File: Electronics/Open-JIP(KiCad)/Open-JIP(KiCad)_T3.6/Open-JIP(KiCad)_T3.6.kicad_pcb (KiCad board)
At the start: 2 copper layers, 61.7 x 35.3 mm, 34 parts, among them J1 EJ503A, J2 Screw_Terminal_01x02, U1 74HC4066D,653, U2 74HC4066D,653, U3 KA7812ETU, U4 OPA320AIDBVT, U5 Teensy3.6

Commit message: finished v0.3 for teensy 3.2 and added gerber files
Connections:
- C5 pad 2: Net-(C5-Pad2) -> GNDA
- U4 pad 2: Net-(C5-Pad2) -> GNDA
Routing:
- net GNDA: track 3.68 -> 11.3 mm
- net Net-(C5-Pad2): track 5.68 -> 0.00 mm
- net (no net): vias 2 -> 1

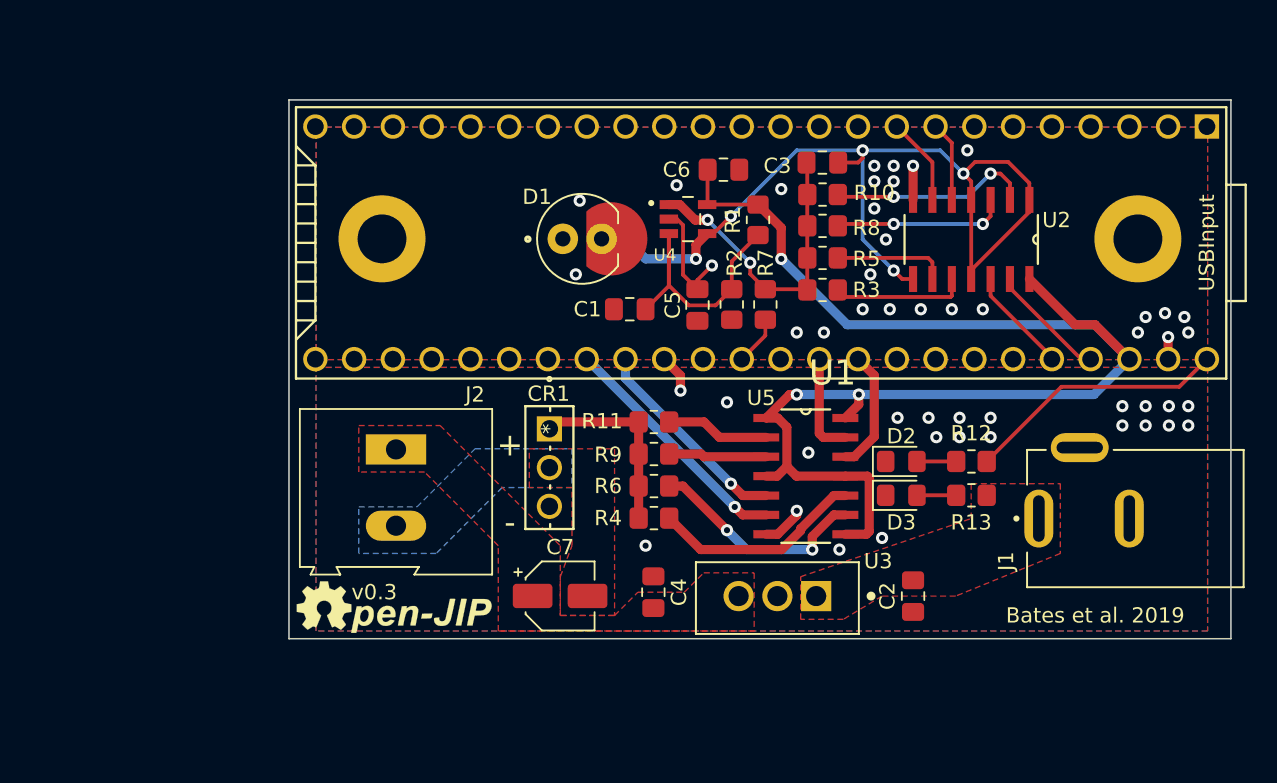
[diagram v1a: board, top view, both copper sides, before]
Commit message: added J-step measuring procedure
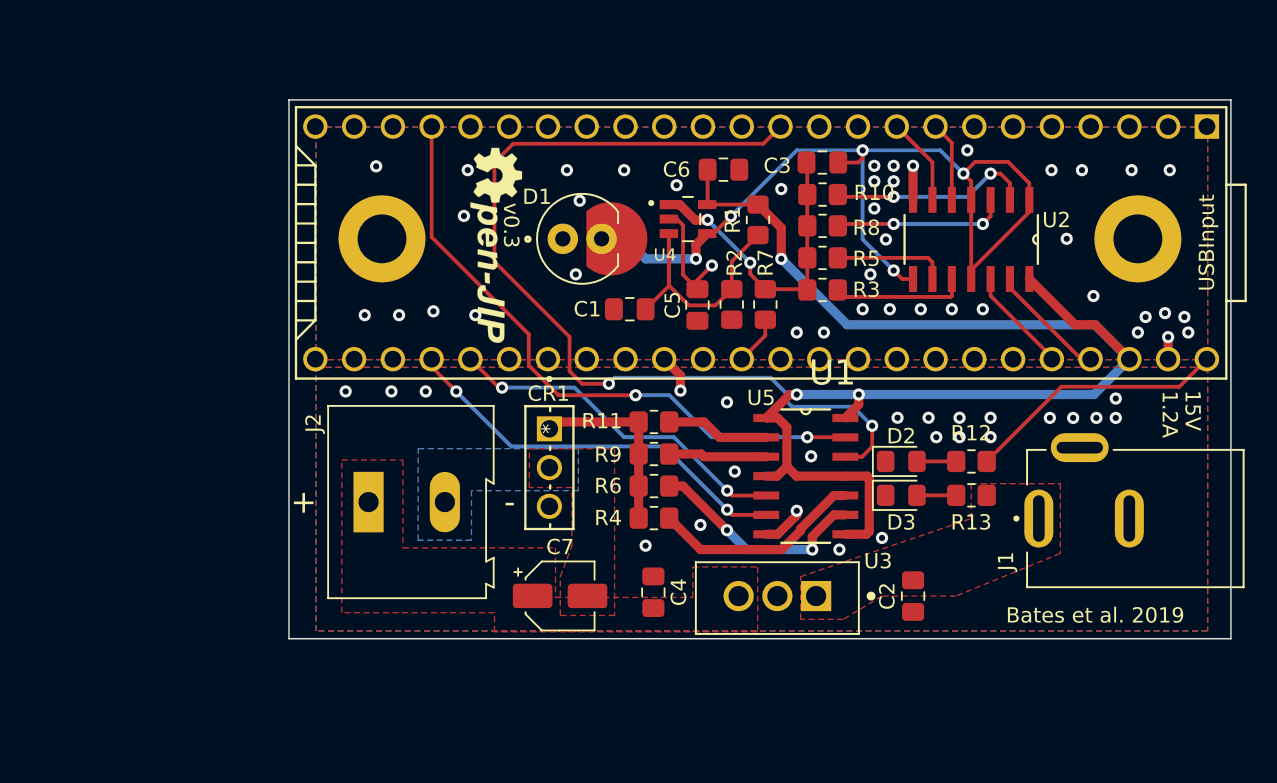
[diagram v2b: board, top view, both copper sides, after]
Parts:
- moved G*** 24.7 mm to (142.8, 82.4), turned to 270 degrees
- moved J2 3.89 mm to (134.5, 99.2), turned to 0 degrees
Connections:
- U5 pad 12: Net-(U5-Pad12) -> ActinicGain4
- U5 pad 21: Net-(U5-Pad21) -> ActinicGain1
- U5 pad 33: Net-(U5-Pad33) -> ActinicGain3
- U5 pad 34: Net-(U5-Pad34) -> ActinicGain2
- U5 pad 37: ActinicGain3 -> Net-(U5-Pad37)
- U5 pad 38: ActinicGain2 -> Net-(U5-Pad38)
- U5 pad 43: ActinicGain1 -> Net-(U5-Pad43)
- U5 pad 44: ActinicGain4 -> Net-(U5-Pad44)
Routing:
- net ActinicGain4: track 7.97 -> 60.8 mm, vias 0 -> 2
- net ActinicGain1: track 6.68 -> 41.0 mm, vias 0 -> 2
- net ActinicGain3: track 16.0 -> 26.4 mm, vias 1 -> 2
- net ActinicGain2: track 13.7 -> 23.1 mm, vias 1 -> 2
- net GNDA: vias 26 -> 41
- net GND: vias 22 -> 24
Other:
- board text added: "1.2A"
- board text added: "15V"

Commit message: od and fluorometer design
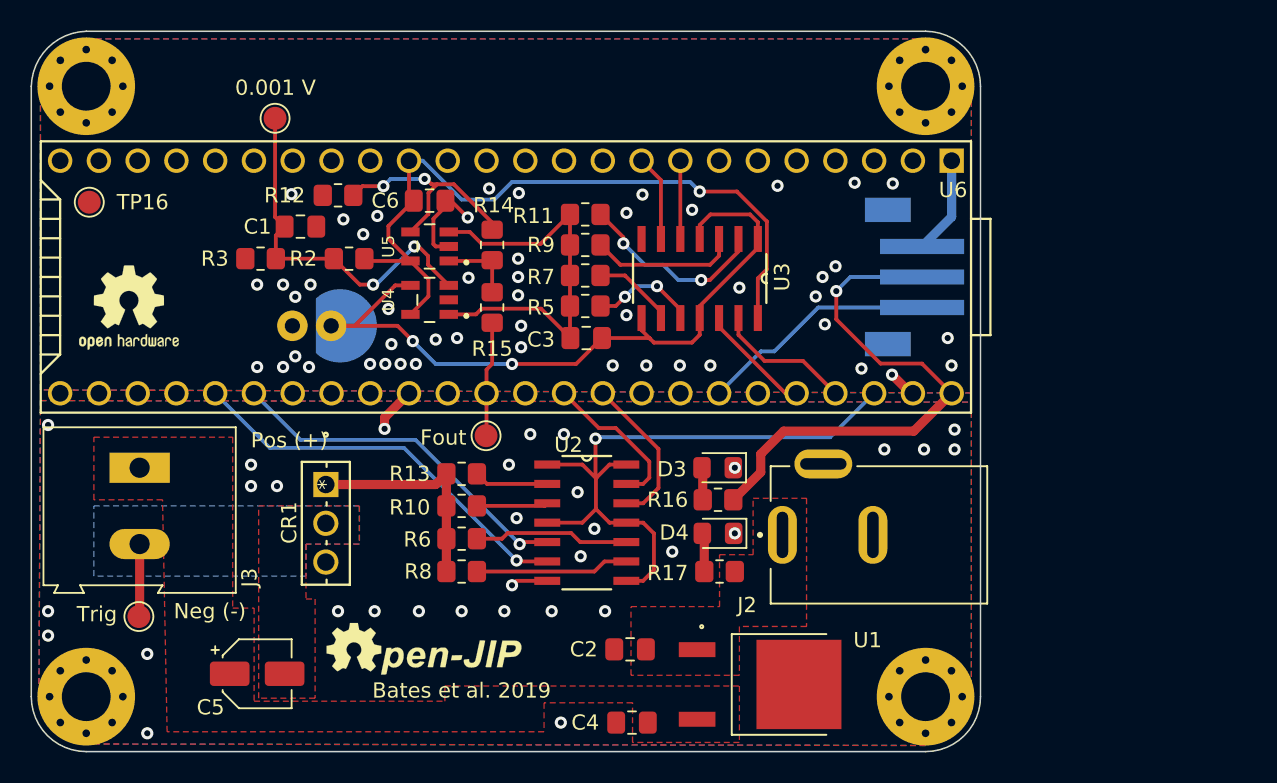
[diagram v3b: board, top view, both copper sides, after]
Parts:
- removed C7: 1uF, Capacitor_SMD:CP_Elec_4x5.4
- removed D1: SFH_213_FA, Additional-parts:SFH_213_FA
- removed J1: EJ503A, Additional-parts:DCJack_MPD_EJ503A
- removed R1: 20K, Resistor_SMD:R_0805_2012Metric_Pad1.20x1.40mm_HandSolder
- removed R4: 8.2K, Resistor_SMD:R_0805_2012Metric_Pad1.20x1.40mm_HandSolder
- removed the REF** at (184.9, 82.0)
- removed the REF** at (135.4, 82.0)
- added 0.001 V: 0.001, TestPoint:TestPoint_Pad_D1.5mm, F.Cu at (128.4, 74.1)
- added D4: LED, LED_SMD:LED_0805_2012Metric_Pad1.15x1.40mm_HandSolder, F.Cu at (157.4, 101.3)
- added Fout: OA-Out, TestPoint:TestPoint_Pad_D1.5mm, F.Cu at (142.2, 94.9)
- added J3: Screw_Terminal_01x02, TerminalBlock:TerminalBlock_Altech_AK300-2_P5.00mm, F.Cu at (119.5, 97.0)
- added J4: B3B-PH-SM4-TB(LF)(SN), Additional-parts:JST_B3B-PH-SM4-TB(LF)(SN), B.Cu at (168.5, 84.5)
- added R14: 50K, Resistor_SMD:R_0805_2012Metric_Pad1.20x1.40mm_HandSolder, F.Cu at (142.6, 82.4)
- added R15: 47, Resistor_SMD:R_0805_2012Metric_Pad1.20x1.40mm_HandSolder, F.Cu at (142.6, 86.5)
- added R16: 1K, Resistor_SMD:R_0805_2012Metric_Pad1.20x1.40mm_HandSolder, F.Cu at (157.4, 99.1)
- added R17: 15K, Resistor_SMD:R_0805_2012Metric_Pad1.20x1.40mm_HandSolder, F.Cu at (157.5, 103.8)
- added REF**: OSHW-Logo2_7.3x6mm_SilkScreen, Symbol:OSHW-Logo2_7.3x6mm_SilkScreen, F.Cu at (118.8, 86.5)
- added REF**: MountingHole_3.2mm_M3_Pad_Via, MountingHole:MountingHole_3.2mm_M3_Pad_Via, F.Cu at (171.0, 112.0)
- added REF**: MountingHole_3.2mm_M3_Pad_Via, MountingHole:MountingHole_3.2mm_M3_Pad_Via, F.Cu at (116.0, 112.0)
- added REF**: MountingHole_3.2mm_M3_Pad_Via, MountingHole:MountingHole_3.2mm_M3_Pad_Via, F.Cu at (171.0, 72.0)
- added REF**: MountingHole_3.2mm_M3_Pad_Via, MountingHole:MountingHole_3.2mm_M3_Pad_Via, F.Cu at (116.0, 72.0)
- added TP16: AGND, TestPoint:TestPoint_Pad_D1.5mm, F.Cu at (116.2, 79.6)
- added Trig: TrigOut, TestPoint:TestPoint_Pad_D1.5mm, F.Cu at (119.5, 106.8)
- added U6: Teensy3.6, Teensy:Teensy35_36, F.Cu at (143.5, 84.5)
- C5: value 100nF -> 0.5uF; footprint Capacitor_SMD:C_0805_2012Metric_Pad1.18x1.45mm_HandSolder -> Capacitor_SMD:CP_Elec_4x5.4
- D2: value LED -> SFH_213_FA; footprint LED_SMD:LED_0805_2012Metric_Pad1.15x1.40mm_HandSolder -> Additional-parts:SFH_213_FA; moved to B.Cu
- J2: value Screw_Terminal_01x02 -> EJ503A; footprint TerminalBlock:TerminalBlock_Altech_AK300-2_P5.00mm -> Additional-parts:DCJack_MPD_EJ503A
- R10: value 1M -> 6.8K
- R11: value 4.3K -> 100K
- R12: value 1K -> 300
- R13: value 15K -> 5.1K
- R2: value 5 -> 20K
- R3: value 3.9M -> 5
- R5: value 3.3M -> 10K
- R6: value 6.8K -> 10K
- R7: value 47 -> 20K
- R8: value 2.3M -> 8.2K
- R9: value 5.1K -> 50K
- U1: value 74HC4066D,653 -> L7806CD2T-TR; footprint Additional-parts:SOIC127P600X175-14N -> Additional-parts:VREG_L7805CDT-TR
- U3: value KA7812ETU -> 74HC4066D,653; footprint TO253P1067X470X2040-3 -> Additional-parts:SOIC127P600X175-14N
- U5: value Teensy3.6 -> OPA320AIDBVT; footprint Teensy:Teensy35_36 -> Additional-parts:SOT95P280X145-5N
- moved R12 45.0 mm to (132.5, 79.2), turned to 0 degrees
- moved D2 39.6 mm to (130.8, 87.7)
- moved C5 37.6 mm to (127.2, 110.5), turned to 0 degrees
- moved R3 36.9 mm to (127.4, 83.3)
- moved R13 33.4 mm to (140.6, 97.4), turned to 0 degrees
- moved R8 32.7 mm to (140.6, 103.8)
- moved U2 31.3 mm to (148.8, 100.6), turned to 0 degrees
- moved R10 31.2 mm to (140.6, 99.5)
- moved J2 29.9 mm to (164.3, 101.4), turned to 90 degrees
- moved G*** 26.9 mm to (138.1, 108.9), turned to 0 degrees
- moved R2 25.3 mm to (133.2, 83.3), turned to 0 degrees
- moved C1 22.2 mm to (130.0, 81.2), turned to 180 degrees
- moved U3 22.2 mm to (156.2, 84.6), turned to 270 degrees
- moved U5 21.7 mm to (138.5, 82.5)
- moved C6 19.4 mm to (138.5, 79.5)
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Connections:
- C2 pad 2: +15V -> +12V
- C5 pad 1: GNDA -> Net-(C4-Pad2)
- C5 pad 2: GNDA -> Net-(C5-Pad2)
- CR1 pad 2: Net-(C7-Pad2) -> Net-(C5-Pad2)
- D2 pad 1: GND -> GNDA
- D2 pad 2: Net-(D2-Pad2) -> /-IN
- J2 pad 1: Net-(C4-Pad2) -> +12V
- J2 pad 2: Net-(C7-Pad2) -> GND
- R10 pad 1: /Out -> /TrigOut
- R11 pad 1: /TrigOut -> /Out
- R12 pad 1: +5V -> GNDA
- R12 pad 2: Net-(D2-Pad2) -> Net-(R12-Pad2)
- R13 pad 1: +15V -> /TrigOut
- R13 pad 2: Net-(D3-Pad2) -> Net-(R13-Pad2)
- R2 pad 1: GNDA -> Net-(C1-Pad2)
- R2 pad 2: Net-(C1-Pad2) -> +3V3
- R3 pad 1: /Out -> GNDA
- R3 pad 2: Net-(R3-Pad2) -> Net-(C1-Pad2)
- R7 pad 1: FluoroRead -> /Out
- R7 pad 2: /Out -> Net-(R7-Pad2)
- R8 pad 1: /Out -> /TrigOut
- R9 pad 1: /TrigOut -> /Out
- U1 pad 1: +3V3 -> +12V
- U1 pad 2: Net-(R11-Pad2) -> Net-(C4-Pad2)
- U1 pad 3: Net-(R9-Pad2) -> GND
- U2 pad 1: /-IN -> +3V3
- U2 pad 10: Net-(R3-Pad2) -> Net-(R6-Pad2)
- U2 pad 11: /-IN -> +3V3
- U2 pad 12: FluoroGain4 -> ActinicGain4
- U2 pad 13: FluoroGain1 -> ActinicGain1
- U2 pad 2: Net-(R10-Pad2) -> Net-(R13-Pad2)
- U2 pad 3: Net-(R8-Pad2) -> Net-(R10-Pad2)
- U2 pad 4: /-IN -> +3V3
- U2 pad 5: FluoroGain2 -> ActinicGain2
- U2 pad 6: FluoroGain3 -> ActinicGain3
- U2 pad 7: GNDA -> GND
- U2 pad 8: /-IN -> +3V3
- U2 pad 9: Net-(R5-Pad2) -> Net-(R8-Pad2)
- U3 pad 1: +15V -> /-IN
- U3 pad 2: GND -> Net-(R11-Pad2)
- U3 pad 3: Net-(C4-Pad2) -> Net-(R9-Pad2)
- U5 pad 2: Net-(U5-Pad2) -> GNDA
- U5 pad 3: Net-(U5-Pad3) -> /Out
- U5 pad 4: Net-(U5-Pad4) -> Net-(R12-Pad2)
- U5 pad 5: Net-(U5-Pad5) -> +3V3
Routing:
- net ActinicGain4: track 60.8 -> 10.2 mm, vias 2 -> 0
- net ActinicGain1: track 41.0 -> 10.2 mm, vias 2 -> 0
- net +5V: track 17.2 -> 35.3 mm, vias 0 -> 1
- net ODEmitter: track 0.00 -> 15.6 mm
- net Net-(R12-Pad2): track 0.00 -> 15.0 mm, vias 0 -> 2
- net Net-(R4-Pad2): track 13.9 -> 0.00 mm
- net /-IN: track 61.3 -> 48.6 mm, vias 5 -> 2
- net Net-(R3-Pad2): track 8.79 -> 0.00 mm
- net Net-(R10-Pad2): track 13.3 -> 4.68 mm, vias 2 -> 0
- net GND: track 5.31 -> 11.8 mm, vias 24 -> 32
- net /Out: track 20.2 -> 26.1 mm, vias 2 -> 0
- net Net-(R11-Pad2): track 6.78 -> 12.6 mm, vias 0 -> 2
- net Net-(C1-Pad2): track 18.3 -> 24.2 mm, vias 0 -> 2
- net Net-(R7-Pad2): track 0.00 -> 5.37 mm
- net Net-(R14-Pad1): track 0.00 -> 4.97 mm
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- added copper zone on F.Cu, net +12V
- added copper zone on B.Cu, net Net-(C5-Pad2)
- added copper zone on F.Cu, net Net-(C5-Pad2)
- removed copper zone on F.Cu, net +15V
- removed copper zone on B.Cu, net Net-(C7-Pad2)
- removed copper zone on F.Cu, net Net-(C7-Pad2)
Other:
- board size 61.7 x 35.3 mm -> 62.2 x 47.2 mm
- board text added: "Neg (-)"
- board text added: "Pos (+)"
- board text removed: "+"
- board text removed: "-"
- board text removed: "1.2A"
- board text removed: "15V"
- board text removed: "v0.3"
